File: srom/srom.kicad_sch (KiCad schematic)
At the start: 12 parts, among them J1 Conn_01x03_Female, U1 4075, U2 74LS245, U3 74LS245, U4 74LS245, U5 Pico-rp2040

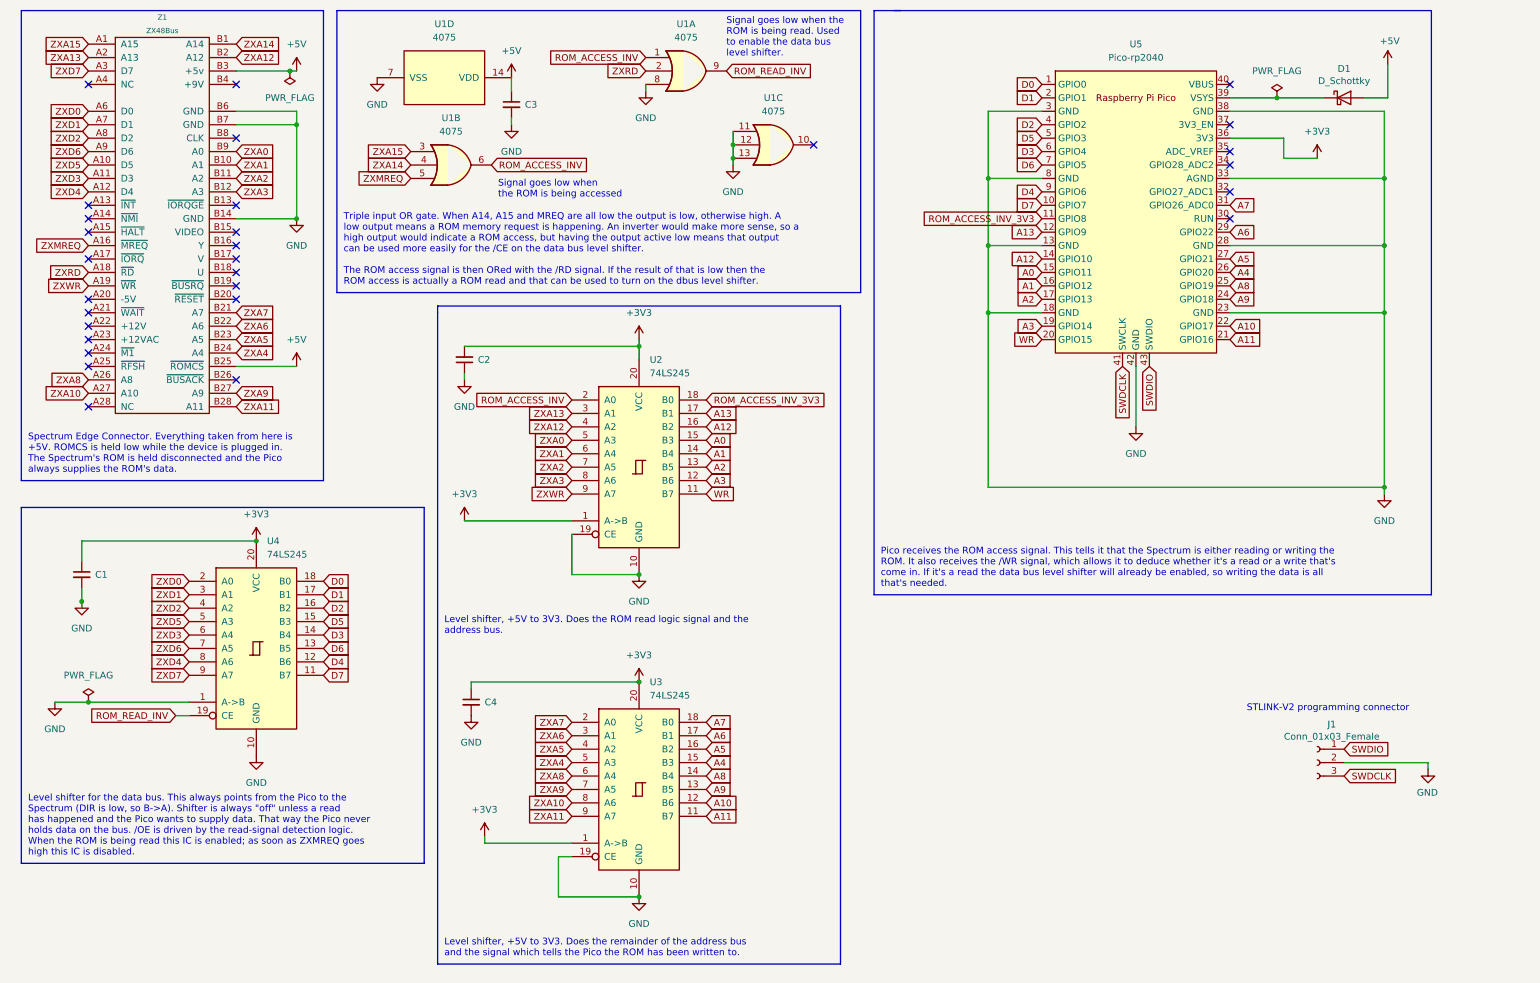
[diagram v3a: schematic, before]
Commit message: hardware mod to add reset feature
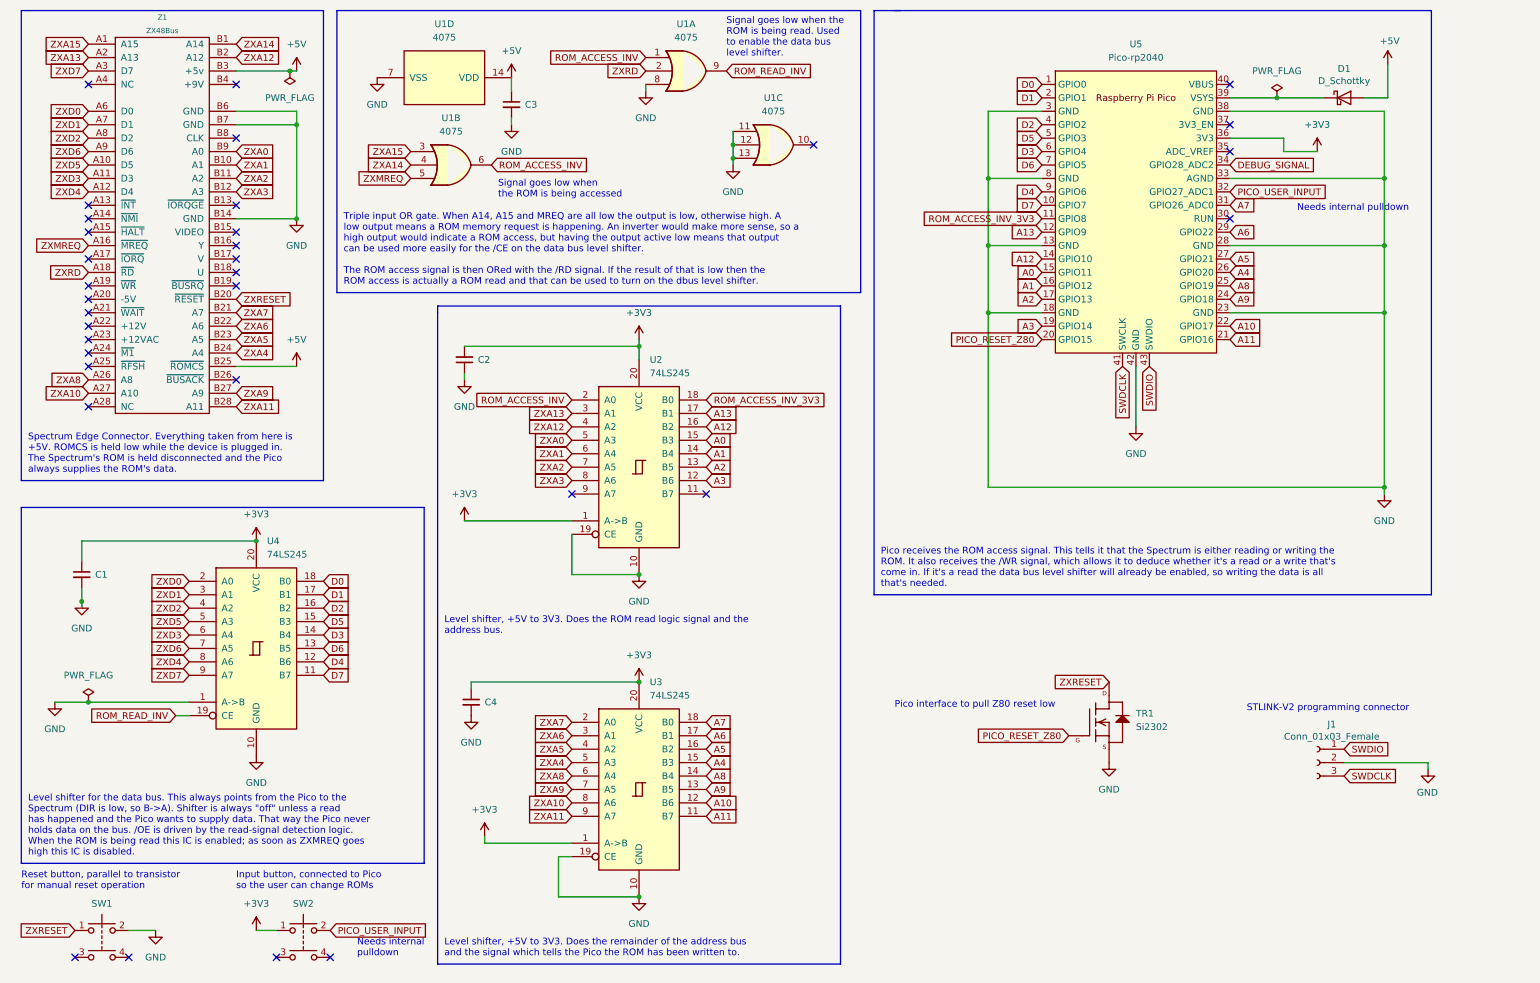
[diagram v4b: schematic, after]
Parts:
- added SW1, SW2: SW_Push_Dual, symbol Switch:SW_Push_Dual
- added TR1: Si2302, Package_TO_SOT_SMD:SOT-23, symbol rp-pico:Si2302CDS-n-channel-New_Library
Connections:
- net +3V3: now also SW2.1
- net GND: now also SW1.2, TR1.2 (S)
- net ZXRESET: now reaches Z1.B20 (~{RESET})
- net ZXRESET: now also SW1.1, TR1.3 (D)
- net PICO_USER_INPUT: now reaches U5.32 (GPIO27_ADC1)
- net PICO_USER_INPUT: now also SW2.2
- net DEBUG_SIGNAL: now reaches U5.34 (GPIO28_ADC2)
- net WR: no longer names the net of U2.11 (B7)
- net WR: no longer U5.20 (GPIO15)
- net ZXWR: no longer names the net of U2.9 (A7)
- net ZXWR: no longer Z1.A19 (~{WR})
- new net PICO_RESET_Z80: TR1.1 (G), U5.20 (GPIO15)
- no-connect marks 29 -> 33
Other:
- note added: "Input button, connected to Pico so the user can change ROMs"
- note added: "Needs internal pulldown"
- note added: "Pico interface to pull Z80 reset low"
- note added: "Reset button, parallel to transistor for manual reset operation"

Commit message: finalise v1.1 schematic
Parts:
- removed SW1, SW2: SW_Push_Dual, symbol Switch:SW_Push_Dual
- removed TR1: Si2302, Package_TO_SOT_SMD:SOT-23, symbol rp-pico:Si2302CDS-n-channel-New_Library
- added Q1: PN2222A, Package_TO_SOT_SMD:SOT-23-3, symbol Transistor_BJT:PN2222A
- added R1: 1K, Resistor_SMD:R_1206_3216Metric_Pad1.30x1.75mm_HandSolder, symbol Device:R_Small
- added SW1: SW_SPST, Button_Switch_THT:SW_PUSH_6mm_H4.3mm, symbol Switch:SW_SPST
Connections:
- net DEBUG_SIGNAL is gone; now on net PICO_RESET_Z80: U5.34 (GPIO28_ADC2)
- net +3V3: now also SW1.1 (A)
- net GND: now also Q1.1 (E)
- net PICO_RESET_Z80: now also R1.1; no longer U5.20 (GPIO15)
- net PICO_USER_INPUT: now also SW1.2 (B)
- net ZXRESET: now also Q1.3 (C)
- new net: Q1.2 (B), R1.2
- no-connect marks 33 -> 30
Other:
- note added: "Level shifter, +5V to 3V3. Does the remainder of the address bus."
- note added: "Pico receives the ROM access signal. This tells it that the Spectrum is either reading or writing the ROM. It treats both the same, so a write to ROM will load a value onto the Pico's data bus pins. It doesn't matter, the level shifter which makes the data bus pins visible to the ZX is only enabled on reads, so ultimately ROM writes don't do anything. Pico has an output to pull the Z80 /RESET lin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"
- note removed: "Level shifter, +5V to 3V3. Does the remainder of the address bus and the signal which tells the Pico the ROM has been written to."
- note removed: "Pico receives the ROM access signal. This tells it that the Spectrum is either reading or writing the ROM. It also receives the /WR signal, which allows it to deduce whether it's a read or a write that's come in. If it's a read the data bus level shifter will already be enabled, so writing the data is all that's needed."
- note removed: "Reset button, parallel to transistor for manual reset operation"

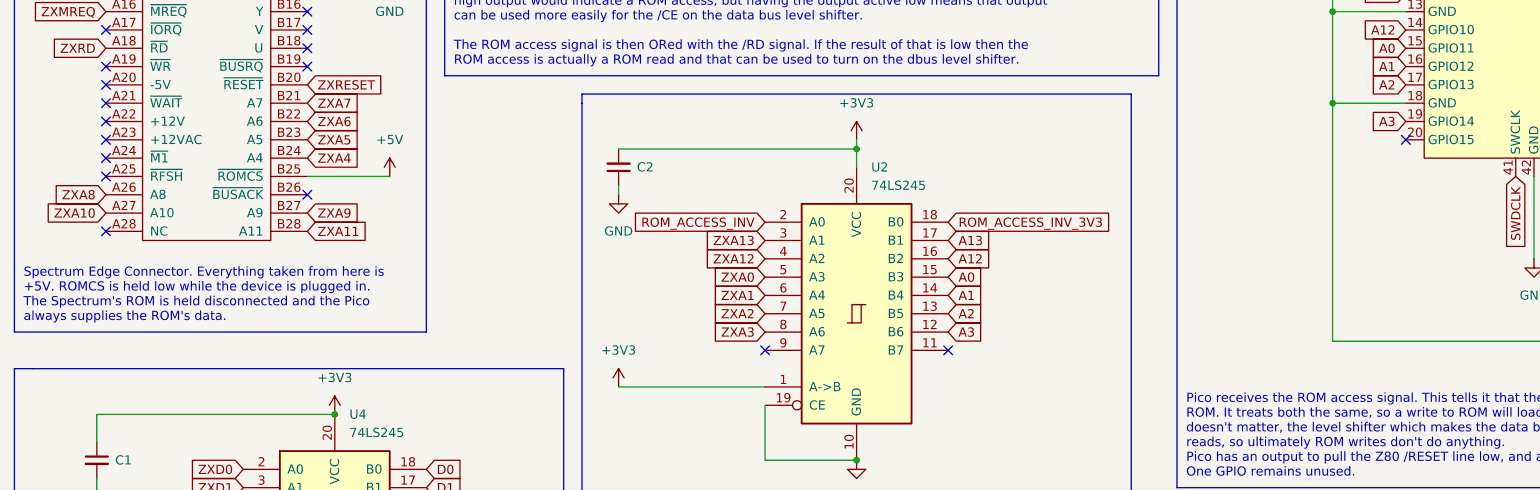
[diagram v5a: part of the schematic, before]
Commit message: Add the /M1 line into the Pico so the IF1 ROM can be used
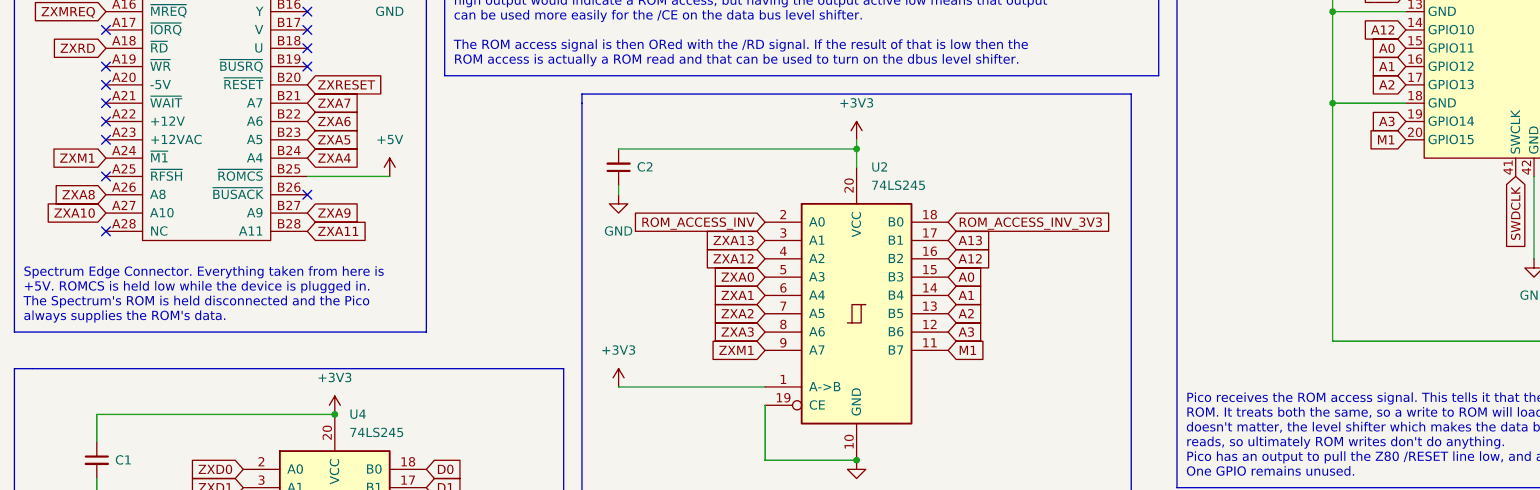
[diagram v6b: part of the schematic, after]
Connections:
- net M1: now reaches U2.11 (B7)
- net M1: now also U5.20 (GPIO15)
- net ZXM1: now reaches U2.9 (A7)
- net ZXM1: now also Z1.A24 (~{M1})
- no-connect marks 30 -> 26
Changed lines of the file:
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@@
   (no_connect (at 26.67 62.23))
   (no_connect (at 54.61 52.07))
-  (no_connect (at 143.51 106.68))
-  (no_connect (at 118.11 106.68))
   (no_connect (at 26.67 74.93))
   (no_connect (at 54.61 39.37))
@@
   (no_connect (at 26.67 82.55))
   (no_connect (at 242.57 54.61))
-  (no_connect (at 207.01 77.47))
   (no_connect (at 26.67 54.61))
-  (no_connect (at 26.67 80.01))
   (no_connect (at 26.67 77.47))
   (no_connect (at 26.67 90.17))
@@
     )
   )
+  (global_label "ZXM1" (shape input) (at 118.11 106.68 180) (fields_autoplaced)
+    (effects (font (size 1.27 1.27)) (justify right))
+    (property "Intersheet References" "${INTERSHEET_REFS}" (id 0) (at 110.6169 106.6006 0)
+      (effects (font (size 1.27 1.27)) (justify right) hide)
+    )
+  )
   (global_label "ZXRESET" (shape input) (at 54.61 69.85 0) (fields_autoplaced)
     (effects (font (size 1.27 1.27)) (justify left))
@@
     (property "Intersheet References" "${INTERSHEET_REFS}" (id 0) (at 148.2212 149.7806 0)
       (effects (font (size 1.27 1.27)) (justify left) hide)
+    )
+  )
+  (global_label "ZXM1" (shape input) (at 26.67 80.01 180) (fields_autoplaced)
+    (effects (font (size 1.27 1.27)) (justify right))
+    (property "Intersheet References" "${INTERSHEET_REFS}" (id 0) (at 19.1769 79.9306 0)
+      (effects (font (size 1.27 1.27)) (justify right) hide)
     )
   )
@@
     )
   )
+  (global_label "M1" (shape input) (at 207.01 77.47 180) (fields_autoplaced)
+    (effects (font (size 1.27 1.27)) (justify right))
+    (property "Intersheet References" "${INTERSHEET_REFS}" (id 0) (at 201.9359 77.3906 0)
+      (effects (font (size 1.27 1.27)) (justify right) hide)
+    )
+  )
   (global_label "ZXD1" (shape input) (at 45.72 125.73 180) (fields_autoplaced)
     (effects (font (size 1.27 1.27)) (justify right))
@@
     )
   )
+  (global_label "M1" (shape input) (at 143.51 106.68 0) (fields_autoplaced)
+    (effects (font (size 1.27 1.27)) (justify left))
+    (property "Intersheet References" "${INTERSHEET_REFS}" (id 0) (at 148.5841 106.6006 0)
+      (effects (font (size 1.27 1.27)) (justify left) hide)
+    )
+  )

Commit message: v1.2 schematic and layout complete
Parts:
- removed Q1: PN2222A, Package_TO_SOT_SMD:SOT-23-3, symbol Transistor_BJT:PN2222A
- added Q1: PMBT2222A, Package_TO_SOT_SMD:TSOT-23_HandSoldering, symbol pmbt2222a:PMBT2222A
- SW1: footprint Button_Switch_THT:SW_PUSH_6mm_H4.3mm -> Button_Switch_THT:SW_Tactile_SKHH_Angled
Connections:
- net GND: now also Q1.2 (E)
- net ZXRESET: now also Q1.3 (C)
- net at R1.2: now also Q1.1 (B)
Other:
- note added: "Pico interface to pull Z80 reset low. Note TTH device differs from SMD device."
- note removed: "Pico interface to pull Z80 reset low"
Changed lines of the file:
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@@
   (title_block
     (title "ZX Spectrum Pico ROM")
-    (date "2023-01-29")
-    (rev "1.1")
+    (date "2023-02-15")
+    (rev "1.2")
   )
   (junction (at 25.4 127) (diameter 0) (color 0 0 0 0)
@@
     (effects (font (size 1.27 1.27)) (justify left bottom))
   )
-  (text "Pico interface to pull\nZ80 reset low" (at 198.12 143.51 180)
+  (text "Pico interface to pull Z80 reset low.\nNote TTH device differs from SMD device."
+    (at 213.36 142.24 180)
     (effects (font (size 1.27 1.27)) (justify right bottom))
   )
@@
     (pin "1")
   )
-  (symbol (lib_id "Transistor_BJT:PN2222A") (at 217.17 151.13 0) (unit 1)
-    (in_bom yes) (on_board yes) (fields_autoplaced)
-    (property "Reference" "Q1" (id 0) (at 222.25 149.8599 0)
-      (effects (font (size 1.27 1.27)) (justify left))
-    )
-    (property "Value" "PN2222A" (id 1) (at 222.25 152.3999 0)
-      (effects (font (size 1.27 1.27)) (justify left))
-    )
-    (property "Footprint" "Package_TO_SOT_SMD:SOT-23-3" (id 2) (at 222.25 153.035 0)
-      (effects (font (size 1.27 1.27) italic) (justify left) hide)
-    )
-    (property "Datasheet" "https://www.onsemi.com/pub/Collateral/PN2222-D.PDF" (id 3) (at 217.17 151.13 0)
-      (effects (font (size 1.27 1.27)) (justify left) hide)
-    )
-    (pin "1")
-    (pin "2")
-    (pin "3")
-  )
   (symbol (lib_id "4xxx:4075") (at 93.98 27.94 270) (mirror x) (unit 4)
     (in_bom yes) (on_board yes) (fields_autoplaced)
@@
     (property "Reference" "SW1" (id 0) (at 26.67 184.15 0))
     (property "Value" "SW_SPST" (id 1) (at 26.67 186.69 0))
-    (property "Footprint" "Button_Switch_THT:SW_PUSH_6mm_H4.3mm" (id 2) (at 26.67 190.5 0)
+    (property "Footprint" "Button_Switch_THT:SW_Tactile_SKHH_Angled" (id 2) (at 26.67 190.5 0)
       (effects (font (size 1.27 1.27)) hide)
     )
@@
     (pin "2")
   )
+  (symbol (lib_id "pmbt2222a:PMBT2222A") (at 217.17 151.13 0) (unit 1)
+    (in_bom yes) (on_board yes) (fields_autoplaced)
+    (property "Reference" "Q1" (id 0) (at 222.25 149.8599 0)
+      (effects (font (size 1.27 1.27)) (justify left))
+    )
+    (property "Value" "PMBT2222A" (id 1) (at 222.25 152.3999 0)
+      (effects (font (size 1.27 1.27)) (justify left))
+    )
+    (property "Footprint" "Package_TO_SOT_SMD:TSOT-23_HandSoldering" (id 2) (at 222.25 153.035 0)
+      (effects (font (size 1.27 1.27) italic) (justify left) hide)
+    )
+    (property "Datasheet" "https://www.mouser.co.uk/ProductDetail/771-PMBT2222A-T-R" (id 3) (at 217.17 151.13 0)
+      (effects (font (size 1.27 1.27)) (justify left) hide)
+    )
+    (pin "1")
+    (pin "2")
+    (pin "3")
+  )
   (symbol (lib_id "Device:R_Small") (at 205.74 151.13 90) (unit 1)
     (in_bom yes) (on_board yes) (fields_autoplaced)
@@
       (reference "J1") (unit 1) (value "Conn_01x03_Female") (footprint "Connector_PinHeader_2.54mm:PinHeader_1x03_P2.54mm_Vertical")
     )
-    (path "/1f0eb14f-70f5-4cb1-a65b-a81ba69b9e8d"
-      (reference "Q1") (unit 1) (value "PN2222A") (footprint "Package_TO_SOT_SMD:SOT-23-3")
+    (path "/bdff7cfd-6ce8-49f1-856c-db2e1e7b73e7"
+      (reference "Q1") (unit 1) (value "PMBT2222A") (footprint "Package_TO_SOT_SMD:TSOT-23_HandSoldering")
     )
     (path "/bf2f21de-f445-4e9c-86ad-edabdf2b112f"
@@
     )
     (path "/20d26426-8b21-4db9-ba1f-50fdd05b5159"
-      (reference "SW1") (unit 1) (value "SW_SPST") (footprint "Button_Switch_THT:SW_PUSH_6mm_H4.3mm")
+      (reference "SW1") (unit 1) (value "SW_SPST") (footprint "Button_Switch_THT:SW_Tactile_SKHH_Angled")
     )
     (path "/43a7bd42-380d-437f-8b75-117d267c89f1"
